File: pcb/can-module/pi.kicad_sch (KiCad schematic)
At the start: 33 parts, among them J16 USB4105, J17 Conn_01x18, J18 Conn_01x18, J3 TC2050, U8 W25Q32JVSSIQ TR, U9 RP2040, Y2 ABM8-272-T3

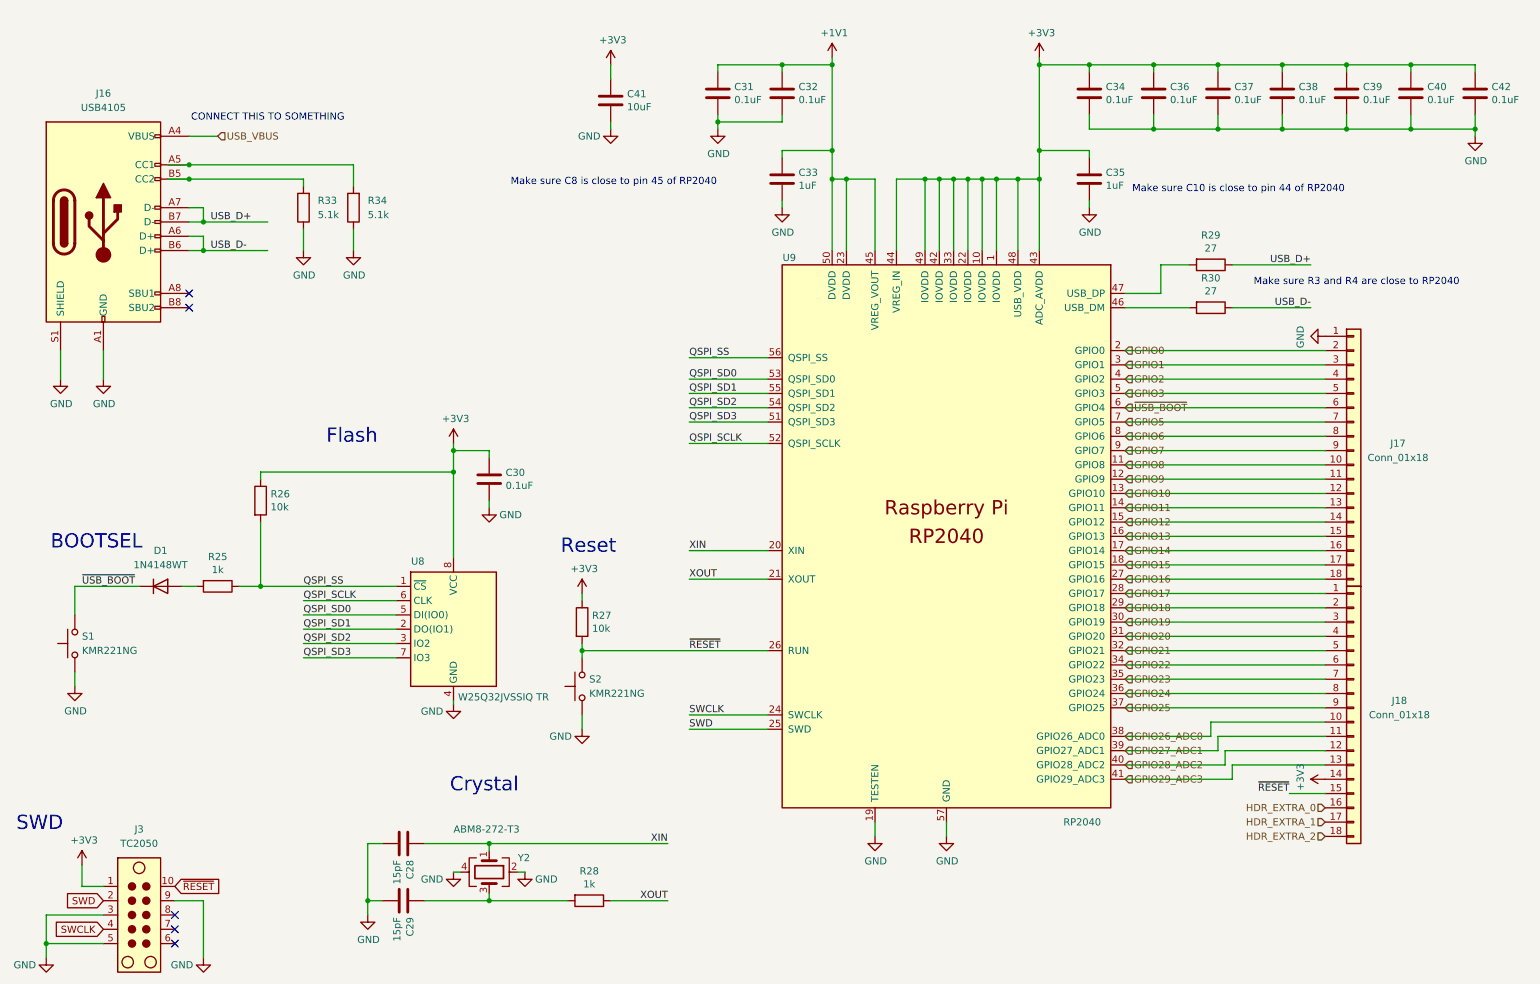
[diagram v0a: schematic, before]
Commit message: Fix ERC errors
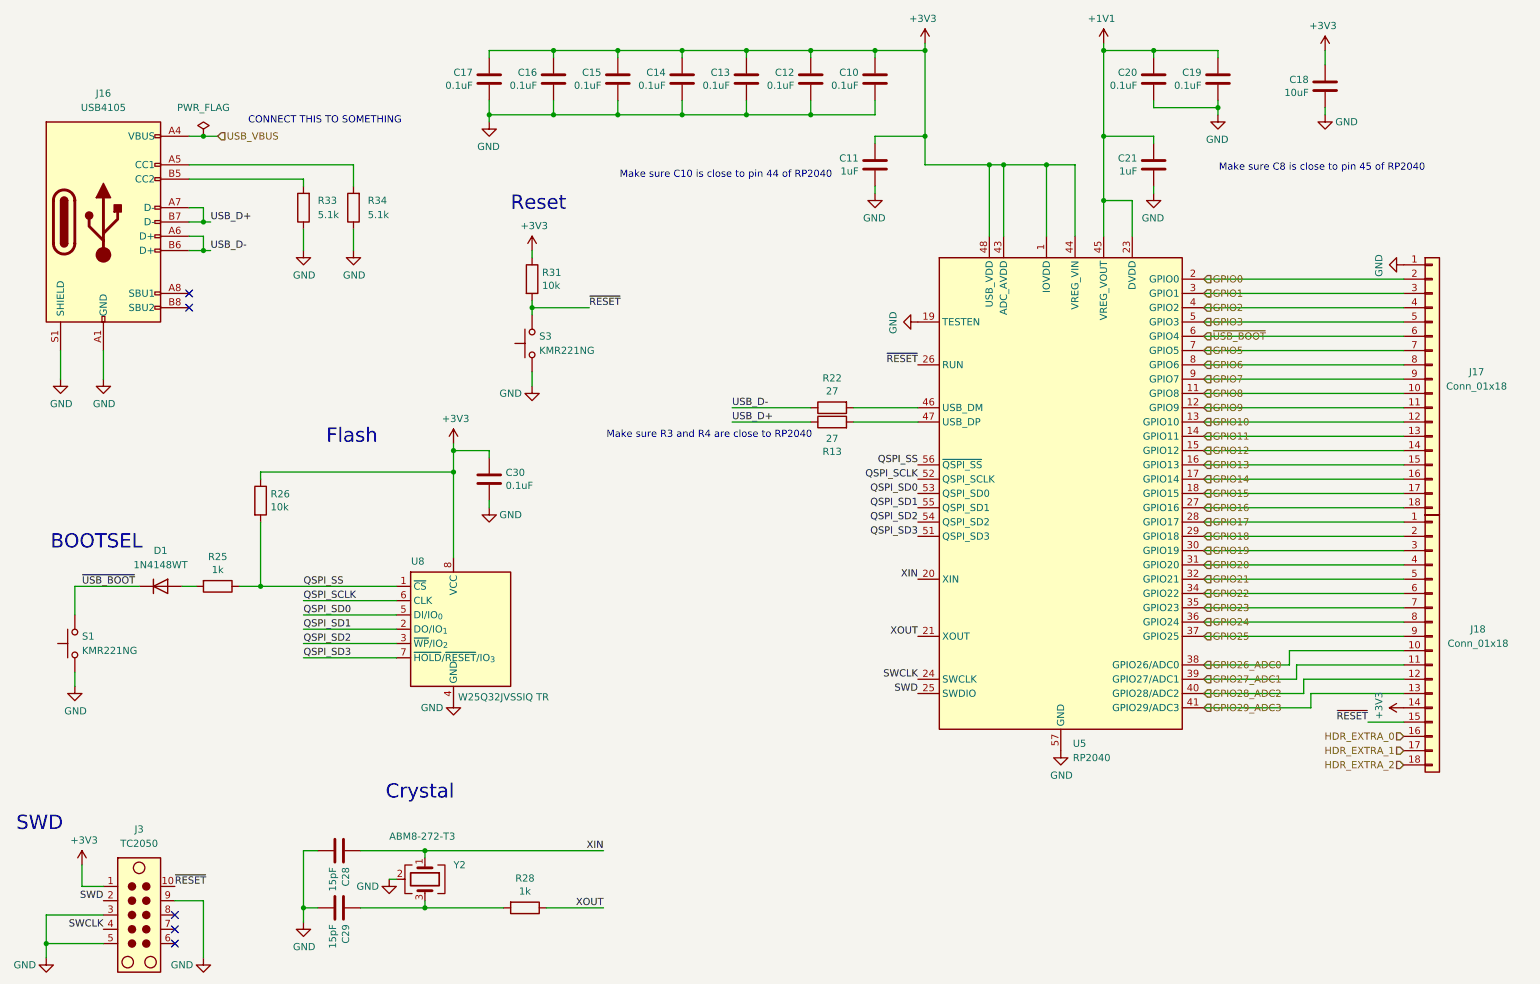
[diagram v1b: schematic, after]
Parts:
- removed C31, C32, C34, C36, C37, C38, C39, C40, C42: 0.1uF, Capacitor_SMD:C_0402_1005Metric, symbol Device:C
- removed C33, C35: 1uF, Capacitor_SMD:C_0402_1005Metric, symbol Device:C
- removed C41: 10uF, Capacitor_SMD:C_0402_1005Metric, symbol Device:C
- removed R27: 10k, Resistor_SMD:R_0402_1005Metric, symbol Device:R
- removed R29, R30: 27, Resistor_SMD:R_0402_1005Metric, symbol Device:R
- removed S2: KMR221NG, Button_Switch_SMD:SW_Push_1P1T_NO_CK_KMR2, symbol Switch:SW_Push
- removed U9: RP2040, RP2040_minimal:RP2040-QFN-56, symbol MCU_RaspberryPi_RP2040:RP2040
- added C10, C12, C13, C14, C15, C16, C17, C19, C20: 0.1uF, Capacitor_SMD:C_0402_1005Metric, symbol Device:C
- added C11, C21: 1uF, Capacitor_SMD:C_0402_1005Metric, symbol Device:C
- added C18: 10uF, Capacitor_SMD:C_0402_1005Metric, symbol Device:C
- added R13, R22: 27, Resistor_SMD:R_0402_1005Metric, symbol Device:R
- added R31: 10k, Resistor_SMD:R_0402_1005Metric, symbol Device:R
- added S3: KMR221NG, Button_Switch_SMD:SW_Push_1P1T_NO_CK_KMR2, symbol Switch:SW_Push
- added U5: RP2040, PCM_JLCPCB:QFN-56-1EP_7x7mm_P0.4mm_EP3.2x3.2mm_ThermalVias, symbol MCU_RaspberryPi:RP2040
- J17, J18: footprint Connector_PinHeader_2.54mm:PinHeader_1x18_P2.54mm_Vertical -> Connector_PinSocket_2.54mm:PinSocket_1x18_P2.54mm_Vertical
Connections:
- net +1V1: now also C19.1, C20.1, C21.1, U5.23 (DVDD), U5.45 (VREG_VOUT), U5.50 (DVDD)
- net +3V3: now also C10.1, C11.1, C12.1, C13.1, C14.1, C15.1, C16.1, C17.1, C18.1, R31.1, U5.1 (IOVDD), U5.10 (IOVDD), U5.22 (IOVDD), U5.33 (IOVDD), U5.42 (IOVDD), U5.43 (ADC_AVDD), U5.44 (VREG_VIN), U5.48 (USB_VDD), U5.49 (IOVDD)
- net GND: now also C10.2, C11.2, C12.2, C13.2, C14.2, C15.2, C16.2, C17.2, C18.2, C19.2, C20.2, C21.2, S3.1, U5.19 (TESTEN), U5.57 (GND)
- net GPIO0: now also U5.2 (GPIO0)
- net GPIO1: now also U5.3 (GPIO1)
- net GPIO10: now also U5.13 (GPIO10)
- net GPIO11: now also U5.14 (GPIO11)
- net GPIO12: now also U5.15 (GPIO12)
- net GPIO13: now also U5.16 (GPIO13)
- net GPIO14: now also U5.17 (GPIO14)
- net GPIO15: now also U5.18 (GPIO15)
- net GPIO16: now also U5.27 (GPIO16)
- net GPIO17: now also U5.28 (GPIO17)
- net GPIO18: now also U5.29 (GPIO18)
- net GPIO19: now also U5.30 (GPIO19)
- net GPIO2: now also U5.4 (GPIO2)
- net GPIO20: now also U5.31 (GPIO20)
- net GPIO21: now also U5.32 (GPIO21)
- net GPIO22: now also U5.34 (GPIO22)
- net GPIO23: now also U5.35 (GPIO23)
- net GPIO24: now also U5.36 (GPIO24)
- net GPIO25: now also U5.37 (GPIO25)
- net GPIO26_ADC0: now also U5.38 (GPIO26/ADC0)
- net GPIO27_ADC1: now also U5.39 (GPIO27/ADC1)
- net GPIO28_ADC2: now also U5.40 (GPIO28/ADC2)
- net GPIO29_ADC3: now also U5.41 (GPIO29/ADC3)
- net GPIO3: now also U5.5 (GPIO3)
- net GPIO5: now also U5.7 (GPIO5)
- net GPIO6: now also U5.8 (GPIO6)
- net GPIO7: now also U5.9 (GPIO7)
- net GPIO8: now also U5.11 (GPIO8)
- net GPIO9: now also U5.12 (GPIO9)
- net QSPI_SCLK: now also U5.52 (QSPI_SCLK)
- net QSPI_SD0: now also U5.53 (QSPI_SD0)
- net QSPI_SD1: now also U5.55 (QSPI_SD1)
- net QSPI_SD2: now also U5.54 (QSPI_SD2)
- net QSPI_SD3: now also U5.51 (QSPI_SD3)
- net QSPI_SS: now also U5.56 (~{QSPI_SS})
- net SWCLK: now also U5.24 (SWCLK)
- net SWD: now also U5.25 (SWDIO)
- net USB_D+: now also R13.1
- net USB_D-: now also R22.1
- net XIN: now also U5.20 (XIN)
- net XOUT: now also U5.21 (XOUT)
- net ~{RESET}: now also R31.2, S3.2, U5.26 (RUN)
- net ~{USB_BOOT}: now also U5.6 (GPIO4)
- new net: R22.2, U5.46 (USB_DM)
- new net: R13.2, U5.47 (USB_DP)
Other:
- moved on the sheet: C28, C29, J17, J18, R28, U8

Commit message: Board layout
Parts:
- U5: footprint PCM_JLCPCB:QFN-56-1EP_7x7mm_P0.4mm_EP3.2x3.2mm_ThermalVias -> Package_DFN_QFN:QFN-56-1EP_7x7mm_P0.4mm_EP3.2x3.2mm; LCSC (none) -> C2040; private KLC_S4.2_VREG_VOUT -> (none)
- renumbered C28 to C10, C19 to C11, C14 to C12, C18 to C13, C15 to C14, C13 to C15, C12 to C17, C17 to C18, C11 to C19, C21 to C20, C20 to C21, C10 to C22, C30 to C23, C29 to C9, J18 to J12, J17 to J13, J16 to J14, J3 to J6, R31 to R14, R28 to R17, R13 to R22, R22 to R23, R33 to R28, R34 to R29, S3 to S1, S1 to S2, U8 to U6, Y2 to Y1
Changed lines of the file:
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@@
 		(dnp no)
 		(fields_autoplaced yes)
-		(property "Reference" "S1"
+		(property "Reference" "S2"
 			(at 27.94 124.4599 90)
 			(effects
@@
 			(project "can-module"
 				(path "/8c0b3d8b-46d3-4173-ab1e-a61765f77d61/d5cb3cf7-15bc-482b-8aab-3380c324c314"
-					(reference "S1")
+					(reference "S2")
 					(unit 1)
 				)
@@
 		(on_board yes)
 		(dnp no)
-		(property "Reference" "C28"
+		(property "Reference" "C10"
 			(at 74.8284 165.481 0)
 			(effects
@@
 			(project "can-module"
 				(path "/8c0b3d8b-46d3-4173-ab1e-a61765f77d61/d5cb3cf7-15bc-482b-8aab-3380c324c314"
-					(reference "C28")
+					(reference "C10")
 					(unit 1)
 				)
@@
 		(on_board yes)
 		(dnp no)
-		(property "Reference" "C17"
+		(property "Reference" "C18"
 			(at 97.409 24.2316 0)
 			(effects
@@
 			(project "can-module"
 				(path "/8c0b3d8b-46d3-4173-ab1e-a61765f77d61/d5cb3cf7-15bc-482b-8aab-3380c324c314"
-					(reference "C17")
+					(reference "C18")
 					(unit 1)
 				)
@@
 		(on_board yes)
 		(dnp no)
-		(property "Reference" "C21"
+		(property "Reference" "C20"
 			(at 215.519 39.4716 0)
 			(effects
@@
 			(project "can-module"
 				(path "/8c0b3d8b-46d3-4173-ab1e-a61765f77d61/d5cb3cf7-15bc-482b-8aab-3380c324c314"
-					(reference "C21")
+					(reference "C20")
 					(unit 1)
 				)
@@
 		(dnp no)
 		(fields_autoplaced yes)
-		(property "Reference" "J3"
+		(property "Reference" "J6"
 			(at 38.1 158.75 0)
 			(effects
@@
 			(project "can-module"
 				(path "/8c0b3d8b-46d3-4173-ab1e-a61765f77d61/d5cb3cf7-15bc-482b-8aab-3380c324c314"
-					(reference "J3")
+					(reference "J6")
 					(unit 1)
 				)
@@
 		(dnp no)
 		(fields_autoplaced yes)
-		(property "Reference" "S3"
+		(property "Reference" "S1"
 			(at 109.22 71.1199 90)
 			(effects
@@
 			(project "can-module"
 				(path "/8c0b3d8b-46d3-4173-ab1e-a61765f77d61/d5cb3cf7-15bc-482b-8aab-3380c324c314"
-					(reference "S3")
+					(reference "S1")
 					(unit 1)
 				)
@@
 		(on_board yes)
 		(dnp no)
-		(property "Reference" "R28"
+		(property "Reference" "R17"
 			(at 106.68 167.4622 90)
 			(effects
@@
 			(project "can-module"
 				(path "/8c0b3d8b-46d3-4173-ab1e-a61765f77d61/d5cb3cf7-15bc-482b-8aab-3380c324c314"
-					(reference "R28")
+					(reference "R17")
 					(unit 1)
 				)
@@
 			)
 		)
-		(property "Footprint" "PCM_JLCPCB:QFN-56-1EP_7x7mm_P0.4mm_EP3.2x3.2mm_ThermalVias"
+		(property "Footprint" "Package_DFN_QFN:QFN-56-1EP_7x7mm_P0.4mm_EP3.2x3.2mm"
 			(at 201.93 99.06 0)
 			(effects
@@
 			)
 		)
-		(property private "KLC_S4.2_DVDD" "Not a standalone power converter; internal on-chip voltage regulator for digital core supply; DVDD is the digital core power supply, should be placed next to voltage regulator output."
-			(at 201.93 101.6 0)
-			(show_name yes)
-			(effects
-				(font
-					(size 1.27 1.27)
-				)
-				(hide yes)
-			)
-		)
-		(property private "KLC_S4.2_VREG_VOUT" "Should be placed next to DVDD."
-			(at 201.93 101.6 0)
-			(show_name yes)
+		(property "LCSC" "C2040"
+			(at 204.0733 143.51 0)
 			(effects
 				(font
@@
 		(on_board yes)
 		(dnp no)
-		(property "Reference" "C20"
+		(property "Reference" "C21"
 			(at 215.519 24.2316 0)
 			(effects
@@
 			(project "can-module"
 				(path "/8c0b3d8b-46d3-4173-ab1e-a61765f77d61/d5cb3cf7-15bc-482b-8aab-3380c324c314"
-					(reference "C20")
+					(reference "C21")
 					(unit 1)
 				)
@@
 		(on_board yes)
 		(dnp no)
-		(property "Reference" "J18"
+		(property "Reference" "J12"
 			(at 276.098 123.19 0)
 			(effects
@@
 			(project "can-module"
 				(path "/8c0b3d8b-46d3-4173-ab1e-a61765f77d61/d5cb3cf7-15bc-482b-8aab-3380c324c314"
-					(reference "J18")
+					(reference "J12")
 					(unit 1)
 				)
@@
 		(on_board yes)
 		(dnp no)
-		(property "Reference" "C14"
+		(property "Reference" "C12"
 			(at 131.699 24.2316 0)
 			(effects
@@
 			(project "can-module"
 				(path "/8c0b3d8b-46d3-4173-ab1e-a61765f77d61/d5cb3cf7-15bc-482b-8aab-3380c324c314"
-					(reference "C14")
+					(reference "C12")
 					(unit 1)
 				)
@@
 		(dnp no)
 		(fields_autoplaced yes)
-		(property "Reference" "R33"
+		(property "Reference" "R28"
 			(at 69.85 46.9899 0)
 			(effects
@@
 			(project "can-module"
 				(path "/8c0b3d8b-46d3-4173-ab1e-a61765f77d61/d5cb3cf7-15bc-482b-8aab-3380c324c314"
-					(reference "R33")
+					(reference "R28")
 					(unit 1)
 				)
@@
 		(dnp no)
 		(fields_autoplaced yes)
-		(property "Reference" "J16"
+		(property "Reference" "J14"
 			(at 31.75 27.94 0)
 			(effects
@@
 			(project "can-module"
 				(path "/8c0b3d8b-46d3-4173-ab1e-a61765f77d61/d5cb3cf7-15bc-482b-8aab-3380c324c314"
-					(reference "J16")
+					(reference "J14")
 					(unit 1)
 				)
@@
 		(on_board yes)
 		(dnp no)
-		(property "Reference" "C29"
+		(property "Reference" "C9"
 			(at 74.8284 175.641 0)
 			(effects
@@
 			(project "can-module"
 				(path "/8c0b3d8b-46d3-4173-ab1e-a61765f77d61/d5cb3cf7-15bc-482b-8aab-3380c324c314"
-					(reference "C29")
+					(reference "C9")
 					(unit 1)
 				)
@@
 		(on_board yes)
 		(dnp no)
-		(property "Reference" "R13"
+		(property "Reference" "R22"
 			(at 161.29 91.6178 90)
 			(effects
@@
 			(project "can-module"
 				(path "/8c0b3d8b-46d3-4173-ab1e-a61765f77d61/d5cb3cf7-15bc-482b-8aab-3380c324c314"
-					(reference "R13")
+					(reference "R22")
 					(unit 1)
 				)
@@
 		(on_board yes)
 		(dnp no)
-		(property "Reference" "R31"
+		(property "Reference" "R14"
 			(at 109.728 59.7916 0)
 			(effects
@@
 			(project "can-module"
 				(path "/8c0b3d8b-46d3-4173-ab1e-a61765f77d61/d5cb3cf7-15bc-482b-8aab-3380c324c314"
-					(reference "R31")
+					(reference "R14")
 					(unit 1)
 				)
@@
 		(on_board yes)
 		(dnp no)
-		(property "Reference" "J17"
+		(property "Reference" "J13"
 			(at 275.844 77.47 0)
 			(effects
@@
 			(project "can-module"
 				(path "/8c0b3d8b-46d3-4173-ab1e-a61765f77d61/d5cb3cf7-15bc-482b-8aab-3380c324c314"
-					(reference "J17")
+					(reference "J13")
 					(unit 1)
 				)
@@
 		(on_board yes)
 		(dnp no)
-		(property "Reference" "C13"
+		(property "Reference" "C15"
 			(at 143.129 24.2316 0)
 			(effects
@@
 			(project "can-module"
 				(path "/8c0b3d8b-46d3-4173-ab1e-a61765f77d61/d5cb3cf7-15bc-482b-8aab-3380c324c314"
-					(reference "C13")
+					(reference "C15")
 					(unit 1)
 				)
@@
 		(dnp no)
 		(fields_autoplaced yes)
-		(property "Reference" "R34"
+		(property "Reference" "R29"
 			(at 78.74 46.9899 0)
 			(effects
@@
 			(project "can-module"
 				(path "/8c0b3d8b-46d3-4173-ab1e-a61765f77d61/d5cb3cf7-15bc-482b-8aab-3380c324c314"
-					(reference "R34")
+					(reference "R29")
 					(unit 1)
 				)
@@
 		(on_board yes)
 		(dnp no)
-		(property "Reference" "C11"
+		(property "Reference" "C19"
 			(at 165.989 39.4716 0)
 			(effects
@@
 			(project "can-module"
 				(path "/8c0b3d8b-46d3-4173-ab1e-a61765f77d61/d5cb3cf7-15bc-482b-8aab-3380c324c314"
-					(reference "C11")
+					(reference "C19")
 					(unit 1)
 				)
@@
 		(on_board yes)
 		(dnp no)
-		(property "Reference" "C30"
+		(property "Reference" "C23"
 			(at 103.251 95.3516 0)
 			(effects
@@
 			(project "can-module"
 				(path "/8c0b3d8b-46d3-4173-ab1e-a61765f77d61/d5cb3cf7-15bc-482b-8aab-3380c324c314"
-					(reference "C30")
+					(reference "C23")
 					(unit 1)
 				)
@@
 		(on_board yes)
 		(dnp no)
-		(property "Reference" "C10"
+		(property "Reference" "C22"
 			(at 165.989 24.2316 0)
 			(effects
@@
 			(project "can-module"
 				(path "/8c0b3d8b-46d3-4173-ab1e-a61765f77d61/d5cb3cf7-15bc-482b-8aab-3380c324c314"
-					(reference "C10")
+					(reference "C22")
 					(unit 1)
 				)
@@
 		(on_board yes)
 		(dnp no)
-		(property "Reference" "C19"
+		(property "Reference" "C11"
 			(at 226.949 24.2316 0)
 			(effects
@@
 			(project "can-module"
 				(path "/8c0b3d8b-46d3-4173-ab1e-a61765f77d61/d5cb3cf7-15bc-482b-8aab-3380c324c314"
-					(reference "C19")
+					(reference "C11")
 					(unit 1)
 				)
@@
 		(on_board yes)
 		(dnp no)
-		(property "Reference" "R22"
+		(property "Reference" "R23"
 			(at 161.29 78.5622 90)
 			(effects
@@
 			(project "can-module"
 				(path "/8c0b3d8b-46d3-4173-ab1e-a61765f77d61/d5cb3cf7-15bc-482b-8aab-3380c324c314"
-					(reference "R22")
+					(reference "R23")
 					(unit 1)
 				)
@@
 		(on_board yes)
 		(dnp no)
-		(property "Reference" "C12"
+		(property "Reference" "C17"
 			(at 154.559 24.2316 0)
 			(effects
@@
 			(project "can-module"
 				(path "/8c0b3d8b-46d3-4173-ab1e-a61765f77d61/d5cb3cf7-15bc-482b-8aab-3380c324c314"
-					(reference "C12")
+					(reference "C17")
 					(unit 1)
 				)
@@
 		(on_board yes)
 		(dnp no)
-		(property "Reference" "U8"
+		(property "Reference" "U6"
 			(at 87.63 111.125 0)
 			(effects
@@
 			(project "can-module"
 				(path "/8c0b3d8b-46d3-4173-ab1e-a61765f77d61/d5cb3cf7-15bc-482b-8aab-3380c324c314"
-					(reference "U8")
+					(reference "U6")
 					(unit 1)
 				)
@@
 		(on_board yes)
 		(dnp no)
-		(property "Reference" "C18"
+		(property "Reference" "C13"
 			(at 245.999 25.5016 0)
 			(effects
@@
 			(project "can-module"
 				(path "/8c0b3d8b-46d3-4173-ab1e-a61765f77d61/d5cb3cf7-15bc-482b-8aab-3380c324c314"
-					(reference "C18")
+					(reference "C13")
 					(unit 1)
 				)
@@
 		(on_board yes)
 		(dnp no)
-		(property "Reference" "C15"
+		(property "Reference" "C14"
 			(at 120.269 24.2316 0)
 			(effects
@@
 			(project "can-module"
 				(path "/8c0b3d8b-46d3-4173-ab1e-a61765f77d61/d5cb3cf7-15bc-482b-8aab-3380c324c314"
-					(reference "C15")
+					(reference "C14")
 					(unit 1)
 				)
@@
 		(on_board yes)
 		(dnp no)
-		(property "Reference" "Y2"
+		(property "Reference" "Y1"
 			(at 93.98 165.1 90)
 			(effects
@@
 			(project "can-module"
 				(path "/8c0b3d8b-46d3-4173-ab1e-a61765f77d61/d5cb3cf7-15bc-482b-8aab-3380c324c314"
-					(reference "Y2")
+					(reference "Y1")
 					(unit 1)
 				)
